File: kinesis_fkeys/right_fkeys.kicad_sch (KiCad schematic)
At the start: 10 parts, among them J1 RIGHT_13_TOP

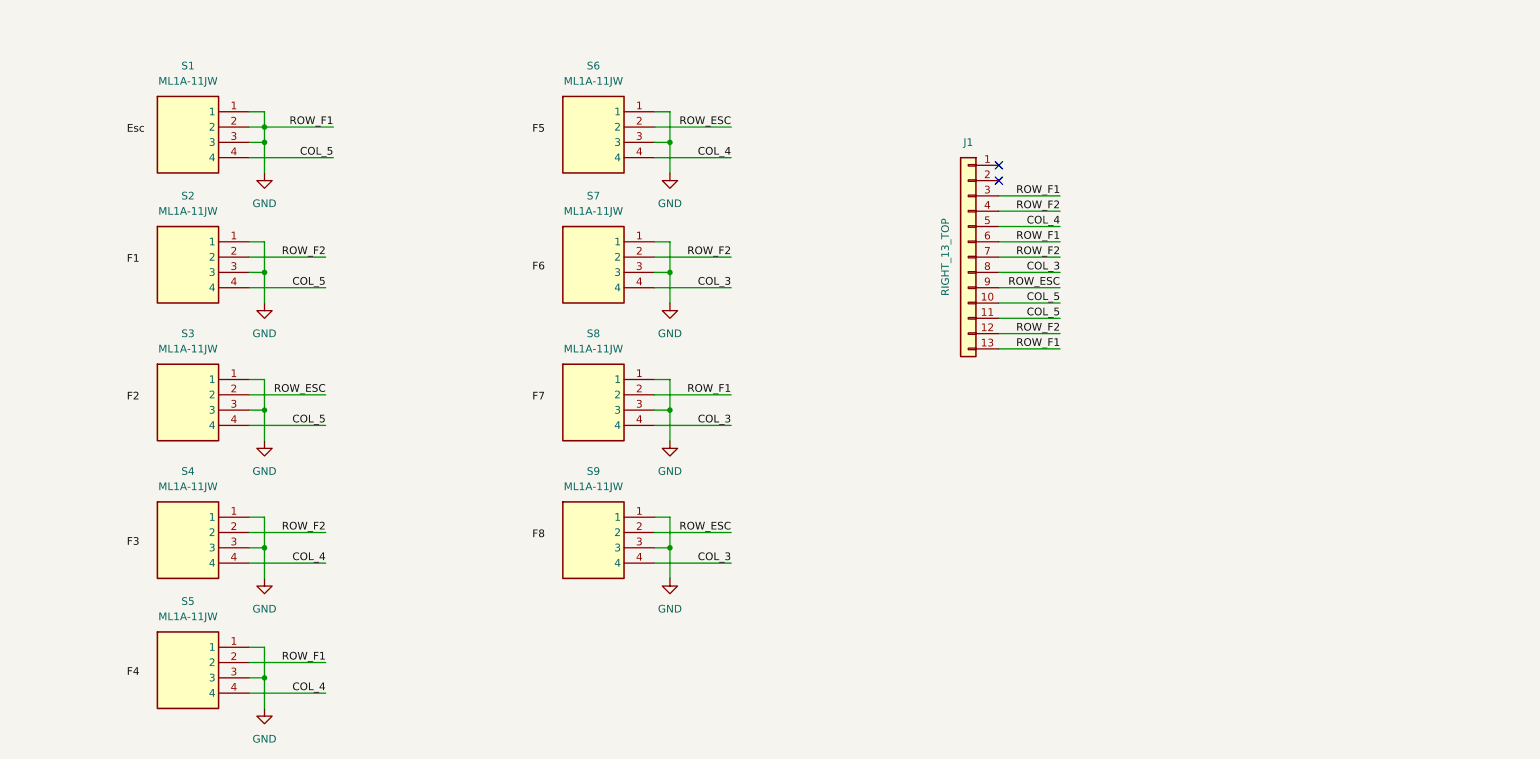
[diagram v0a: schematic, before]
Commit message: buttons schematics verified and placed on the pcb on exact spots
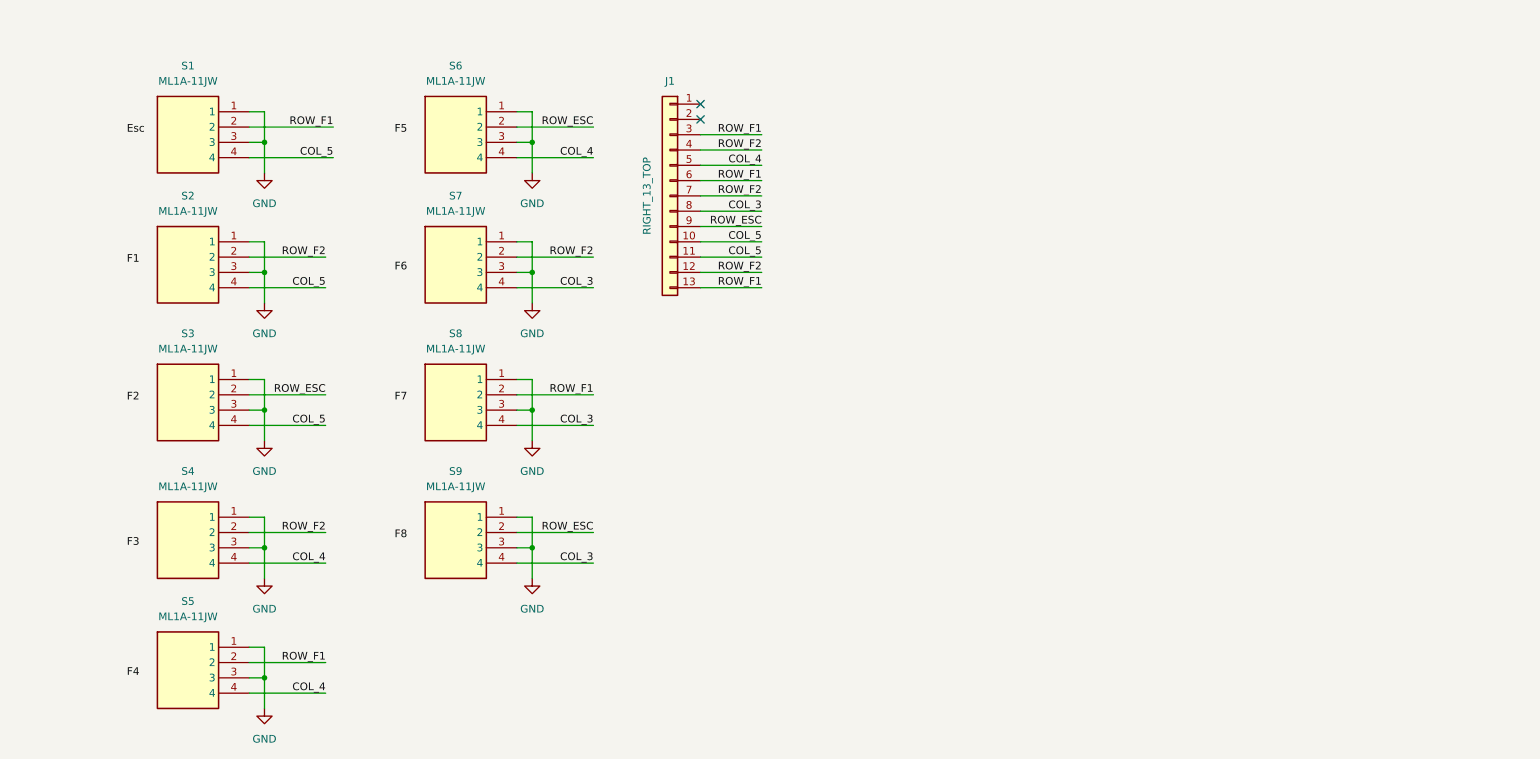
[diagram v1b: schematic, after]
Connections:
- net GND: no longer J1.13 (Pin_13), J1.3 (Pin_3), J1.6 (Pin_6), S1.2, S5.2, S8.2
- new net ROW_F1: J1.13 (Pin_13), J1.3 (Pin_3), J1.6 (Pin_6), S1.2, S5.2, S8.2
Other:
- moved on the sheet: J1, S6, S7, S8, S9

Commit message: added diods againts ghosting on the both PCBs
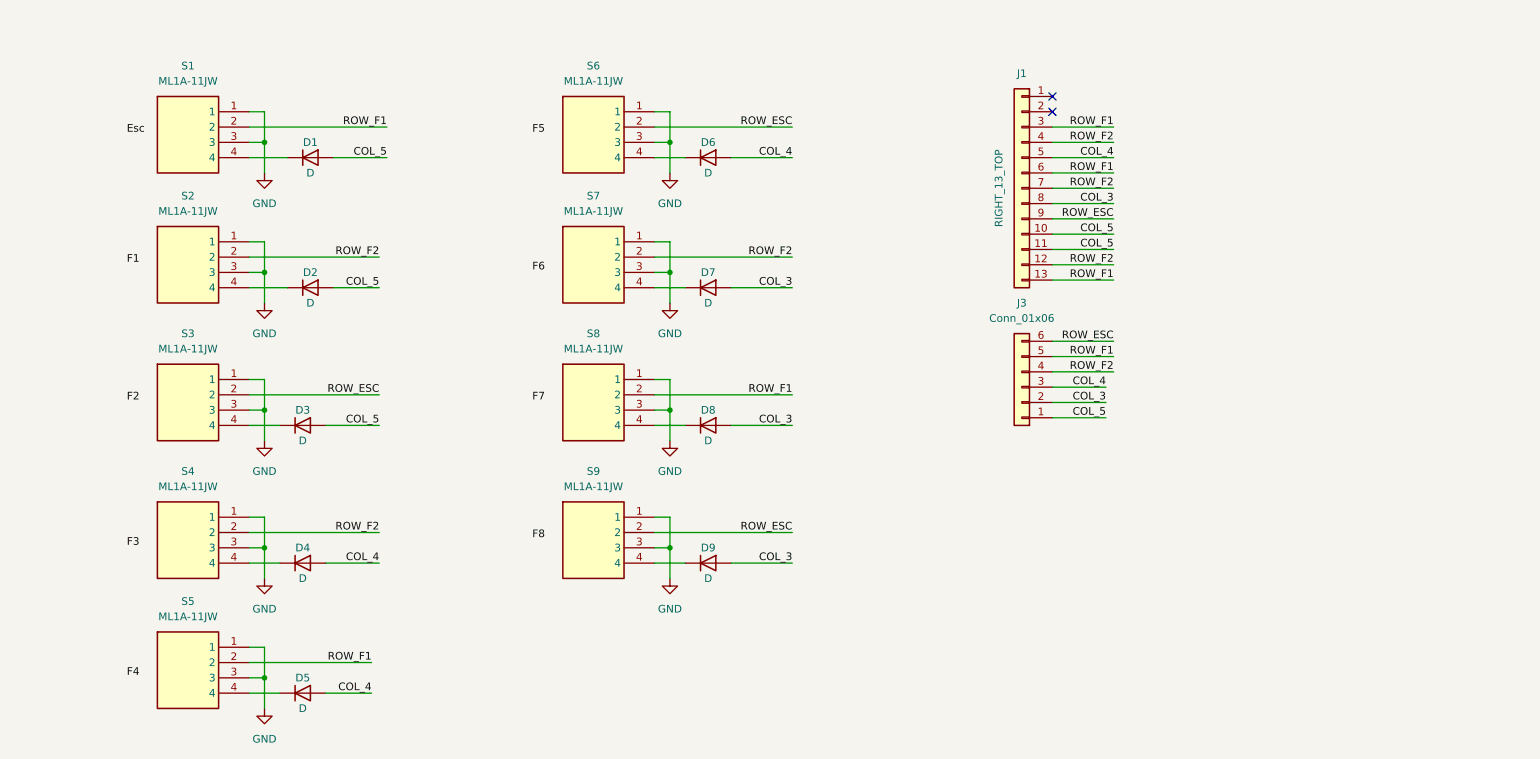
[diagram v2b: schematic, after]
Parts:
- added D1, D2, D3, D4, D5, D6, D7, D8, D9: D, Diode_SMD:D_MiniMELF_Handsoldering, symbol Device:D
- added J3: Conn_01x06, symbol Connector_Generic:Conn_01x06
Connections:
- net COL_3: now also D7.2 (A), D8.2 (A), D9.2 (A), J3.2 (Pin_2); no longer S7.4, S8.4, S9.4
- net COL_4: now also D4.2 (A), D5.2 (A), D6.2 (A), J3.3 (Pin_3); no longer S4.4, S5.4, S6.4
- net COL_5: now also D1.2 (A), D2.2 (A), D3.2 (A), J3.1 (Pin_1); no longer S1.4, S2.4, S3.4
- net ROW_ESC: now also J3.6 (Pin_6)
- net ROW_F1: now also J3.5 (Pin_5)
- net ROW_F2: now also J3.4 (Pin_4)
- new net: D1.1 (K), S1.4
- new net: D3.1 (K), S3.4
- new net: D5.1 (K), S5.4
- new net: D6.1 (K), S6.4
- new net: D8.1 (K), S8.4
- new net: D4.1 (K), S4.4
- new net: D7.1 (K), S7.4
- new net: D2.1 (K), S2.4
- new net: D9.1 (K), S9.4
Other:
- moved on the sheet: J1, S6, S7, S8, S9

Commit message: added TE 84953 6 pin connectors to reduce amount of tracks
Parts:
- J3: footprint (none) -> dodo_conn:84953-6
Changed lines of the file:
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@@
       (effects (font (size 1.27 1.27)))
     )
-    (property "Footprint" "" (at 191.77 82.55 0)
+    (property "Footprint" "dodo_conn:84953-6" (at 191.77 82.55 0)
       (effects (font (size 1.27 1.27)) hide)
     )

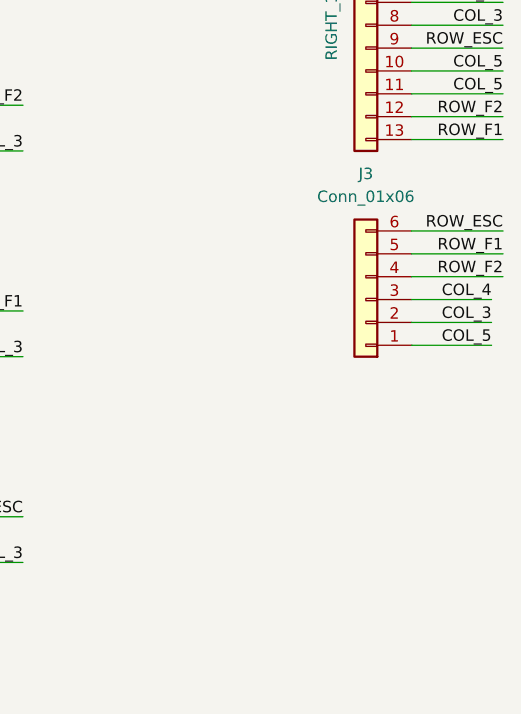
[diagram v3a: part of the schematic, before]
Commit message: fixed wrong amount pins on the footprint and sorted pinout on the connectors
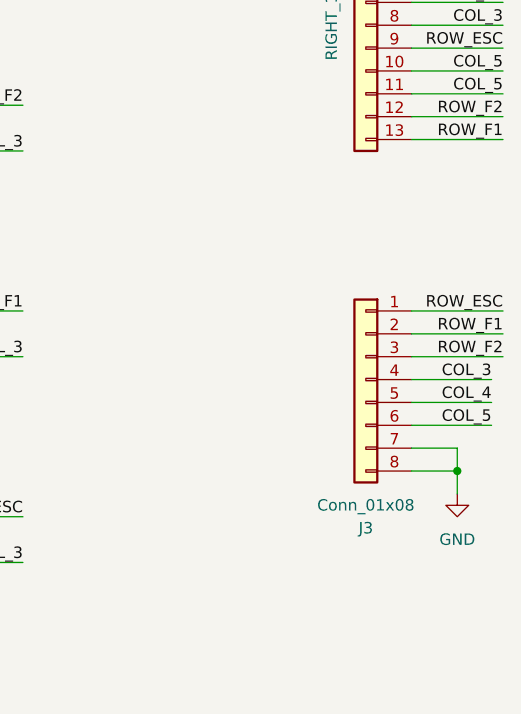
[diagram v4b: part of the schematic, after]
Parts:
- removed J3: Conn_01x06, dodo_conn:84953-6, symbol Connector_Generic:Conn_01x06
- added J3: Conn_01x08, dodo_conn:84953-6, symbol Connector_Generic:Conn_01x08
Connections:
- net COL_3: now also J3.4 (Pin_4)
- net COL_4: now also J3.5 (Pin_5)
- net COL_5: now also J3.6 (Pin_6)
- net GND: now also J3.7 (Pin_7), J3.8 (Pin_8)
- net ROW_ESC: now also J3.1 (Pin_1)
- net ROW_F1: now also J3.2 (Pin_2)
- net ROW_F2: now also J3.3 (Pin_3)
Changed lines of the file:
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@@
   (junction (at 133.35 41.91) (diameter 0) (color 0 0 0 0)
+  )
+  (junction (at 201.93 101.6) (diameter 0) (color 0 0 0 0)
   )
   (junction (at 133.35 109.22) (diameter 0) (color 0 0 0 0)
@@
     (stroke (width 0) (type default))
   )
-  (wire (pts (xy 196.85 85.09) (xy 205.74 85.09))
+  (wire (pts (xy 196.85 93.98) (xy 205.74 93.98))
     (stroke (width 0) (type default))
   )
@@
     (stroke (width 0) (type default))
   )
-  (wire (pts (xy 196.85 87.63) (xy 205.74 87.63))
+  (wire (pts (xy 196.85 96.52) (xy 205.74 96.52))
     (stroke (width 0) (type default))
   )
@@
     (stroke (width 0) (type default))
   )
-  (wire (pts (xy 196.85 82.55) (xy 205.74 82.55))
+  (wire (pts (xy 196.85 91.44) (xy 205.74 91.44))
+    (stroke (width 0) (type default))
+  )
+  (wire (pts (xy 201.93 101.6) (xy 201.93 104.14))
     (stroke (width 0) (type default))
   )
@@
     (stroke (width 0) (type default))
   )
+  (wire (pts (xy 196.85 101.6) (xy 201.93 101.6))
+    (stroke (width 0) (type default))
+  )
   (wire (pts (xy 133.35 41.91) (xy 133.35 46.99))
     (stroke (width 0) (type default))
@@
     (stroke (width 0) (type default))
   )
-  (wire (pts (xy 196.85 80.01) (xy 207.01 80.01))
-    (stroke (width 0) (type default))
-  )
-  (wire (pts (xy 196.85 74.93) (xy 207.01 74.93))
+  (wire (pts (xy 196.85 88.9) (xy 207.01 88.9))
+    (stroke (width 0) (type default))
+  )
+  (wire (pts (xy 196.85 83.82) (xy 207.01 83.82))
     (stroke (width 0) (type default))
   )
@@
     (stroke (width 0) (type default))
   )
-  (wire (pts (xy 196.85 77.47) (xy 207.01 77.47))
+  (wire (pts (xy 196.85 86.36) (xy 207.01 86.36))
     (stroke (width 0) (type default))
   )
@@
   )
   (wire (pts (xy 63.5 81.28) (xy 66.04 81.28))
+    (stroke (width 0) (type default))
+  )
+  (wire (pts (xy 196.85 99.06) (xy 201.93 99.06))
+    (stroke (width 0) (type default))
+  )
+  (wire (pts (xy 201.93 99.06) (xy 201.93 101.6))
     (stroke (width 0) (type default))
   )
@@
     (effects (font (size 1.27 1.27)) (justify right bottom))
   )
-  (label "COL_3" (at 205.74 85.09 180) (fields_autoplaced)
+  (label "COL_3" (at 205.74 91.44 180) (fields_autoplaced)
     (effects (font (size 1.27 1.27)) (justify right bottom))
   )
@@
     (effects (font (size 1.27 1.27)) (justify right bottom))
   )
-  (label "ROW_ESC" (at 207.01 74.93 180) (fields_autoplaced)
+  (label "ROW_ESC" (at 207.01 83.82 180) (fields_autoplaced)
     (effects (font (size 1.27 1.27)) (justify right bottom))
   )
@@
     (effects (font (size 1.27 1.27)) (justify right bottom))
   )
-  (label "COL_4" (at 205.74 82.55 180) (fields_autoplaced)
+  (label "COL_4" (at 205.74 93.98 180) (fields_autoplaced)
     (effects (font (size 1.27 1.27)) (justify right bottom))
   )
@@
     (effects (font (size 1.27 1.27)) (justify right bottom))
   )
-  (label "ROW_F1" (at 207.01 77.47 180) (fields_autoplaced)
+  (label "ROW_F1" (at 207.01 86.36 180) (fields_autoplaced)
     (effects (font (size 1.27 1.27)) (justify right bottom))
   )
@@
     (effects (font (size 1.27 1.27)) (justify right bottom))
   )
-  (label "COL_5" (at 205.74 87.63 180) (fields_autoplaced)
+  (label "COL_5" (at 205.74 96.52 180) (fields_autoplaced)
     (effects (font (size 1.27 1.27)) (justify right bottom))
   )
@@
     (effects (font (size 1.27 1.27)) (justify right bottom))
   )
-  (label "ROW_F2" (at 207.01 80.01 180) (fields_autoplaced)
+  (label "ROW_F2" (at 207.01 88.9 180) (fields_autoplaced)
     (effects (font (size 1.27 1.27)) (justify right bottom))
   )
@@
     )
   )
+  (symbol (lib_id "Connector_Generic:Conn_01x08") (at 191.77 91.44 0) (mirror y) (unit 1)
+    (exclude_from_sim no) (in_bom yes) (on_board yes) (dnp no)
+    (property "Reference" "J3" (at 191.77 107.95 0)
+      (effects (font (size 1.27 1.27)))
+    )
+    (property "Value" "Conn_01x08" (at 191.77 105.41 0)
+      (effects (font (size 1.27 1.27)))
+    )
+    (property "Footprint" "dodo_conn:84953-6" (at 191.77 91.44 0)
+      (effects (font (size 1.27 1.27)) hide)
+    )
+    (property "Datasheet" "~" (at 191.77 91.44 0)
+      (effects (font (size 1.27 1.27)) hide)
+    )
+    (property "Description" "Generic connector, single row, 01x08, script generated (kicad-library-utils/schlib/autogen/connector/)" (at 191.77 91.44 0)
+      (effects (font (size 1.27 1.27)) hide)
+    )
+    (pin "2")
+    (pin "1")
+    (pin "4")
+    (pin "6")
+    (pin "3")
+    (pin "8")
+    (pin "7")
+    (pin "5")
+    (instances
+      (project "kinesis_fkeys"
+        (path "/06886ccb-17ec-482e-a853-bf4276494c0a/106b8080-7c92-4036-9b29-d3ff48894255"
+          (reference "J3") (unit 1)
+        )
+      )
+    )
+  )
   (symbol (lib_id "Device:D") (at 139.7 44.45 0) (unit 1)
     (exclude_from_sim no) (in_bom yes) (on_board yes) (dnp no)
@@
     )
   )
+  (symbol (lib_id "power:GND") (at 201.93 104.14 0) (unit 1)
+    (exclude_from_sim no) (in_bom yes) (on_board yes) (dnp no) (fields_autoplaced)
+    (property "Reference" "#PWR019" (at 201.93 110.49 0)
+      (effects (font (size 1.27 1.27)) hide)
+    )
+    (property "Value" "GND" (at 201.93 109.22 0)
+      (effects (font (size 1.27 1.27)))
+    )
+    (property "Footprint" "" (at 201.93 104.14 0)
+      (effects (font (size 1.27 1.27)) hide)
+    )
+    (property "Datasheet" "" (at 201.93 104.14 0)
+      (effects (font (size 1.27 1.27)) hide)
+    )
+    (property "Description" "Power symbol creates a global label with name \"GND\" , ground" (at 201.93 104.14 0)
+      (effects (font (size 1.27 1.27)) hide)
+    )
+    (pin "1")
+    (instances
+      (project "kinesis_fkeys"
+        (path "/06886ccb-17ec-482e-a853-bf4276494c0a/106b8080-7c92-4036-9b29-d3ff48894255"
+          (reference "#PWR019") (unit 1)
+        )
+      )
+    )
+  )
   (symbol (lib_id "dodo-buttons:ML1A-11JW") (at 53.34 107.95 0) (unit 1)
     (exclude_from_sim no) (in_bom yes) (on_board yes) (dnp no)
@@
         )
       )
-    )
-  )
-  (symbol (lib_id "Connector_Generic:Conn_01x06") (at 191.77 82.55 180) (unit 1)
-    (exclude_from_sim no) (in_bom yes) (on_board yes) (dnp no) (fields_autoplaced)
-    (property "Reference" "J3" (at 191.77 68.58 0)
-      (effects (font (size 1.27 1.27)))
-    )
-    (property "Value" "Conn_01x06" (at 191.77 71.12 0)
-      (effects (font (size 1.27 1.27)))
-    )
-    (property "Footprint" "dodo_conn:84953-6" (at 191.77 82.55 0)
-      (effects (font (size 1.27 1.27)) hide)
-    )
-    (property "Datasheet" "~" (at 191.77 82.55 0)
-      (effects (font (size 1.27 1.27)) hide)
-    )
-    (property "Description" "Generic connector, single row, 01x06, script generated (kicad-library-utils/schlib/autogen/connector/)" (at 191.77 82.55 0)
-      (effects (font (size 1.27 1.27)) hide)
-    )
-    (pin "6")
-    (pin "1")
-    (pin "2")
-    (pin "5")
-    (pin "3")
-    (pin "4")
-    (instances
-      (project "kinesis_fkeys"
-        (path "/06886ccb-17ec-482e-a853-bf4276494c0a/106b8080-7c92-4036-9b29-d3ff48894255"
-          (reference "J3") (unit 1)
-        )
-      )
